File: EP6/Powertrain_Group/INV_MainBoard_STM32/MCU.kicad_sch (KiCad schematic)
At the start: 73 parts, among them J15 STDC14, J4 MSD-4-A, SW1 TS-1187A-B-A-B, SW2 TS-1187A-B-A-B, SW3 TS-1187A-B-A-B, U1 STM32H743ZITx, U23 REF3133AIDBZR, Y1 48MHz YF4048M00033T8188103, Y2 32.768kHz Q13FC13500004

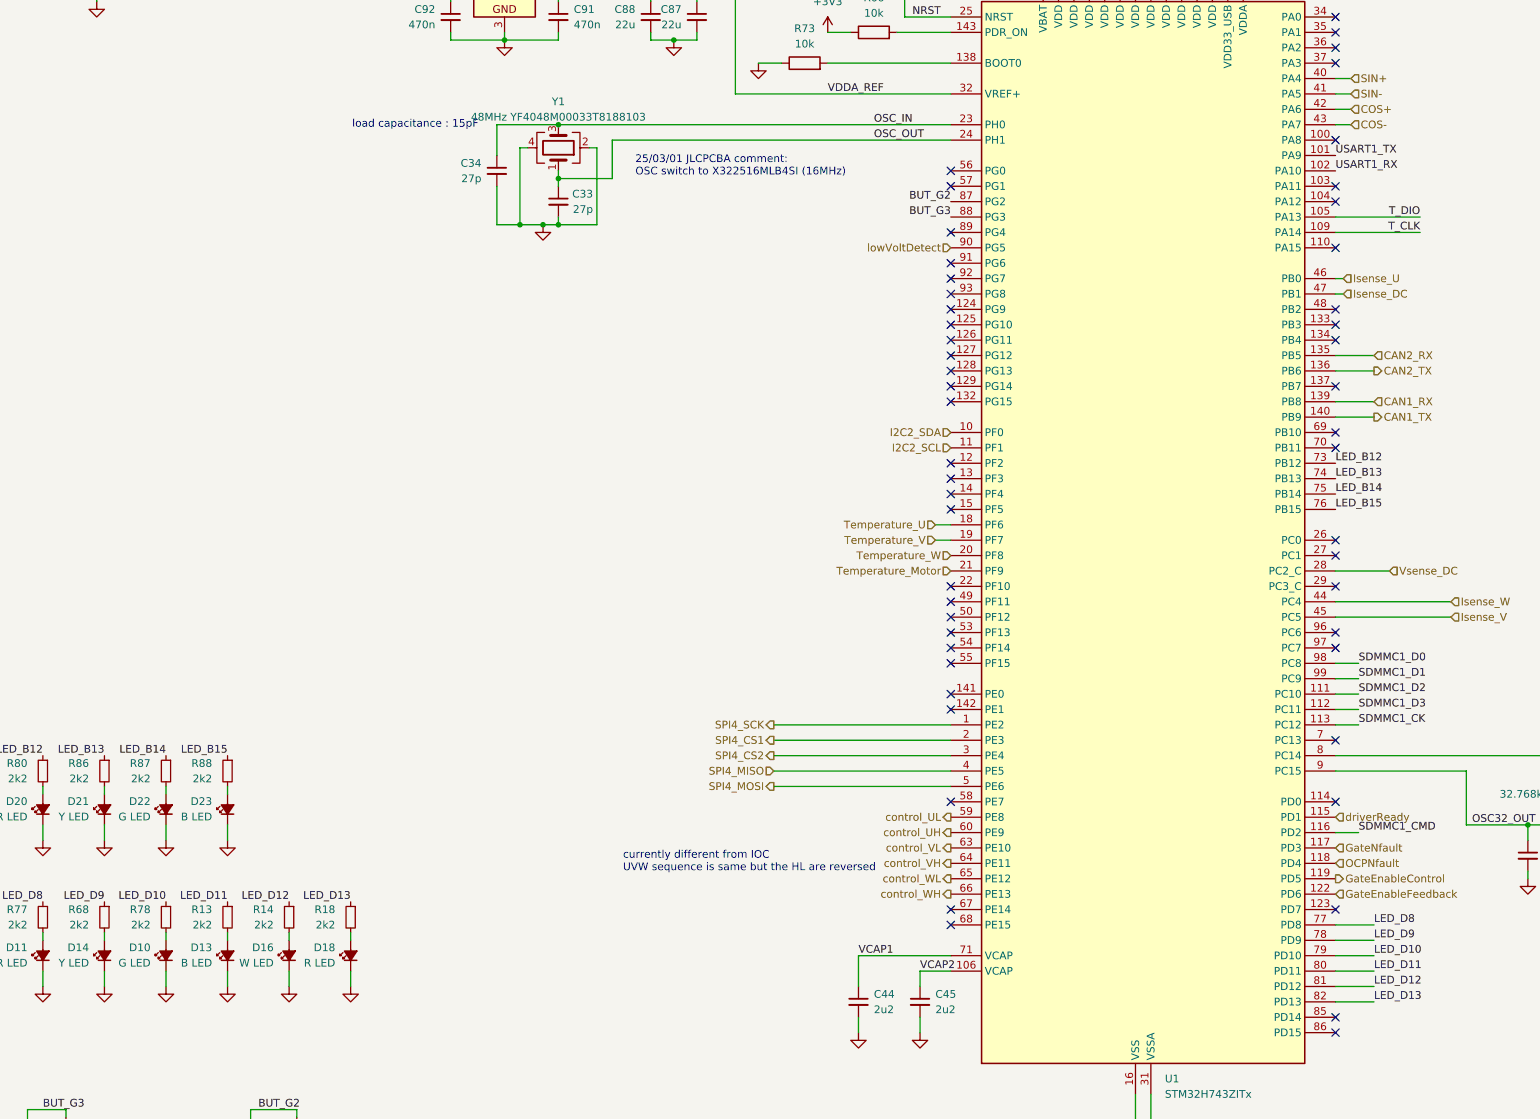
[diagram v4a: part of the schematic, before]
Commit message: update INV_MainBoard_STM32 to V3.0
PCB: INV_MainBoard_STM32 V3.0
V3.0 remove low volte trig
     add RC filt for OCP, OTP
     dedicated OTP, OCP pull down gate enable
     pending: fault hardware OTP/OCP latch
     pending: add QSPI DRAM
     use JST PH
     exterinal pull up for flt, ready
     fix CAN1, 2 label on board
     use 1k, 2k for encoder divider
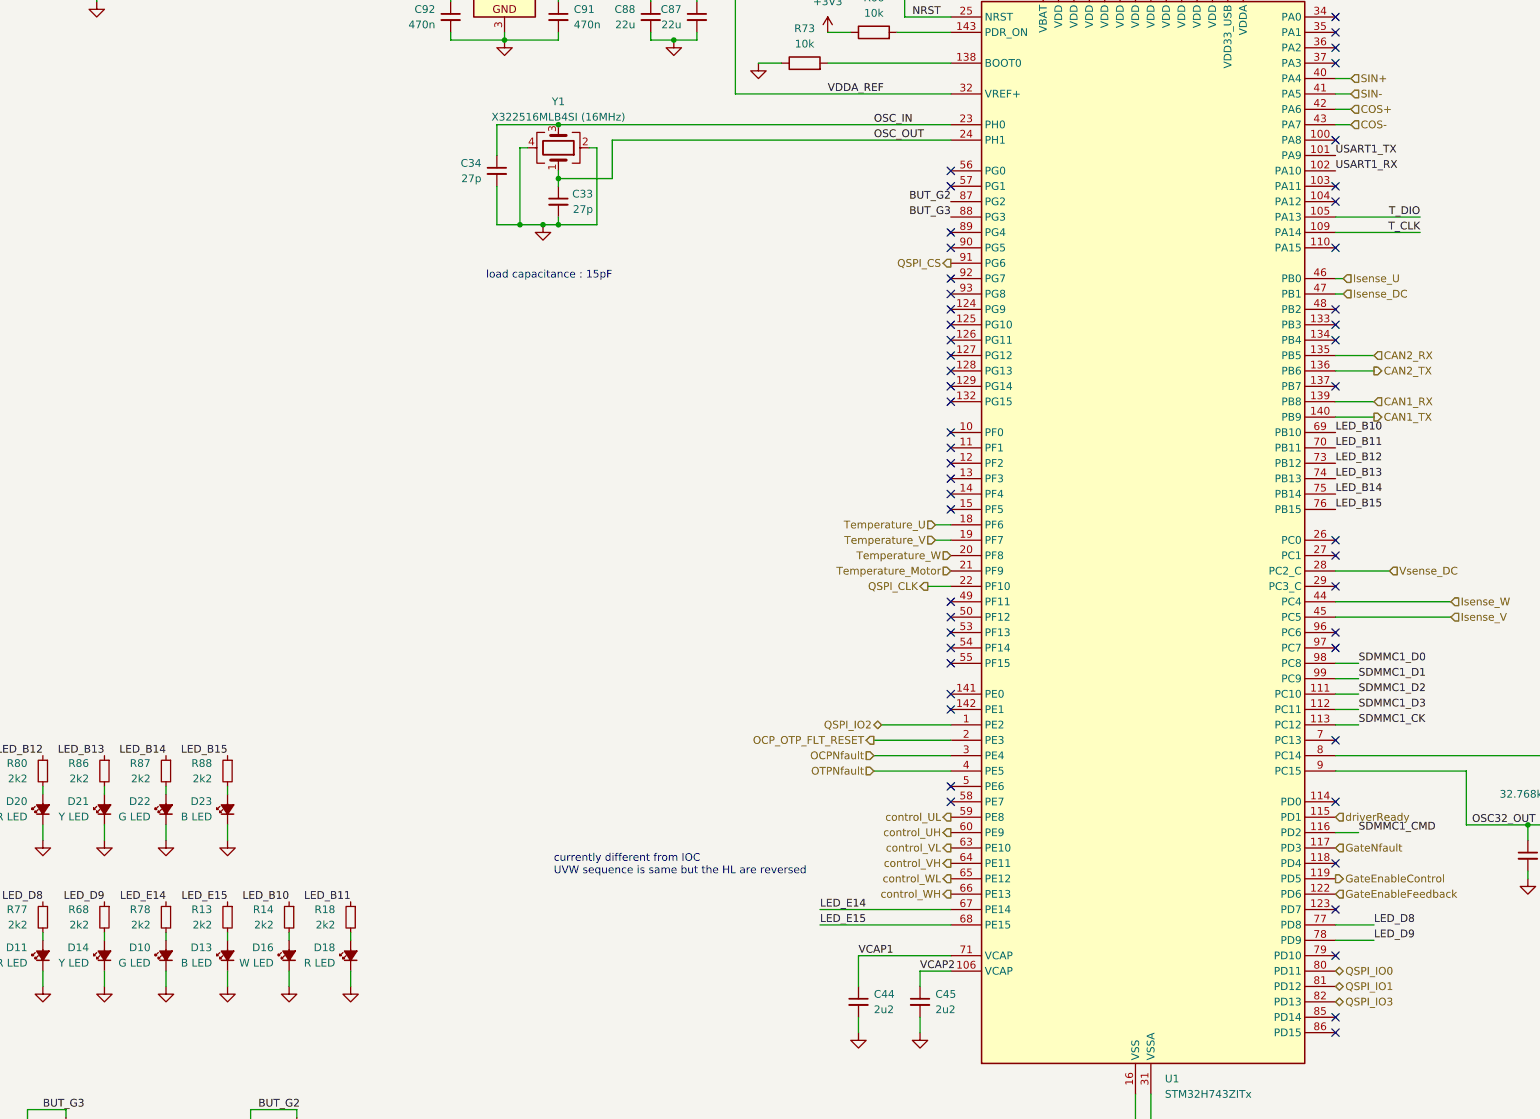
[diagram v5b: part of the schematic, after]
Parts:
- J4: footprint MSD4A -> SamacSys_Parts_EP6:MSD4A
- Y1: value 48MHz YF4048M00033T8188103 -> X322516MLB4SI (16MHz)
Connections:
- net SPI4_CS2 is gone; now on net OCPNfault: U1.3 (PE4)
- net OCPNfault: no longer U1.118 (PD4)
- net QSPI_CLK: now reaches U1.22 (PF10)
- net LED_E14: now reaches U1.67 (PE14)
- net LED_E14: now also R78.1
- net LED_E15: now reaches U1.68 (PE15)
- net LED_E15: now also R13.1
- net LED_B10: now reaches U1.69 (PB10)
- net LED_B10: now also R14.1
- net LED_B11: now reaches U1.70 (PB11)
- net LED_B11: now also R18.1
- net QSPI_CS: now reaches U1.91 (PG6)
- net I2C2_SCL: no longer names the net of U1.11 (PF1)
- net I2C2_SDA: no longer names the net of U1.10 (PF0)
- net LED_D10: no longer names the net of U1.79 (PD10)
- net LED_D10: no longer R78.1
- net LED_D11 renamed QSPI_IO0
- net QSPI_IO0: no longer R13.1
- net LED_D12 renamed QSPI_IO1
- net QSPI_IO1: no longer R14.1
- net LED_D13 renamed QSPI_IO3
- net QSPI_IO3: no longer R18.1
- net SPI4_CS1 renamed OCP_OTP_FLT_RESET
- net SPI4_MISO renamed OTPNfault
- net SPI4_MOSI: no longer names the net of U1.5 (PE6)
- net SPI4_SCK renamed QSPI_IO2
- net lowVoltDetect: no longer names the net of U1.90 (PG5)
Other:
- note removed: "25/03/01 JLCPCBA comment: OSC switch to X322516MLB4SI (16MHz)"

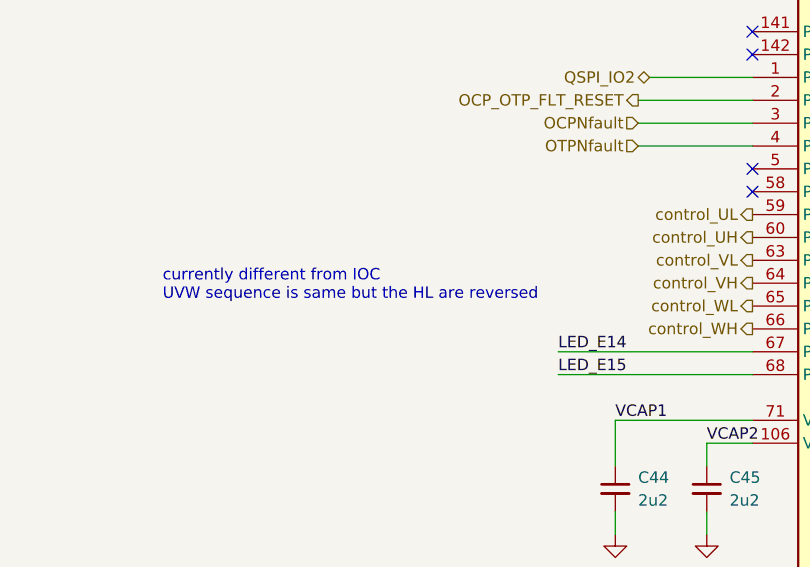
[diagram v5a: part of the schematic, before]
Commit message: update INV_MainBoard_STM32 to V3.1
V3.1 fix R93 to 100R
     add led for OCP, OTP flt
     add default Res for OTP threshold
     add gnd pins for testing
     fix latch circuit
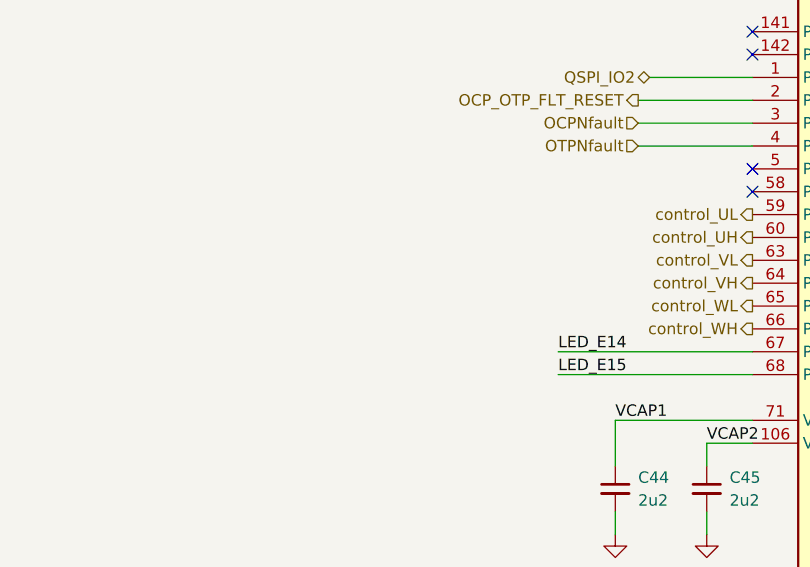
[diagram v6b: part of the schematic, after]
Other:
- note removed: "currently different from IOC UVW sequence is same but the HL are reversed"
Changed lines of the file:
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@@
 	(title_block
 		(title "INV_MainBoard_STM32")
-		(date "2025-06-29")
-		(rev "3.0")
+		(date "2025-06-30")
+		(rev "3.1")
 		(company "NTURacing Team")
 		(comment 1 "郭哲明 Jack Kuo")
@@
 		)
 	)
-	(text "currently different from IOC\nUVW sequence is same but the HL are reversed"
-		(exclude_from_sim no)
-		(at 108.458 220.472 0)
-		(effects
-			(font
-				(size 1.27 1.27)
-			)
-			(justify left bottom)
-		)
-	)
